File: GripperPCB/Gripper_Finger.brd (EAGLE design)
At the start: 26.6 x 20 mm, 6 parts, among them IC1 ATMEGA328PB-AU

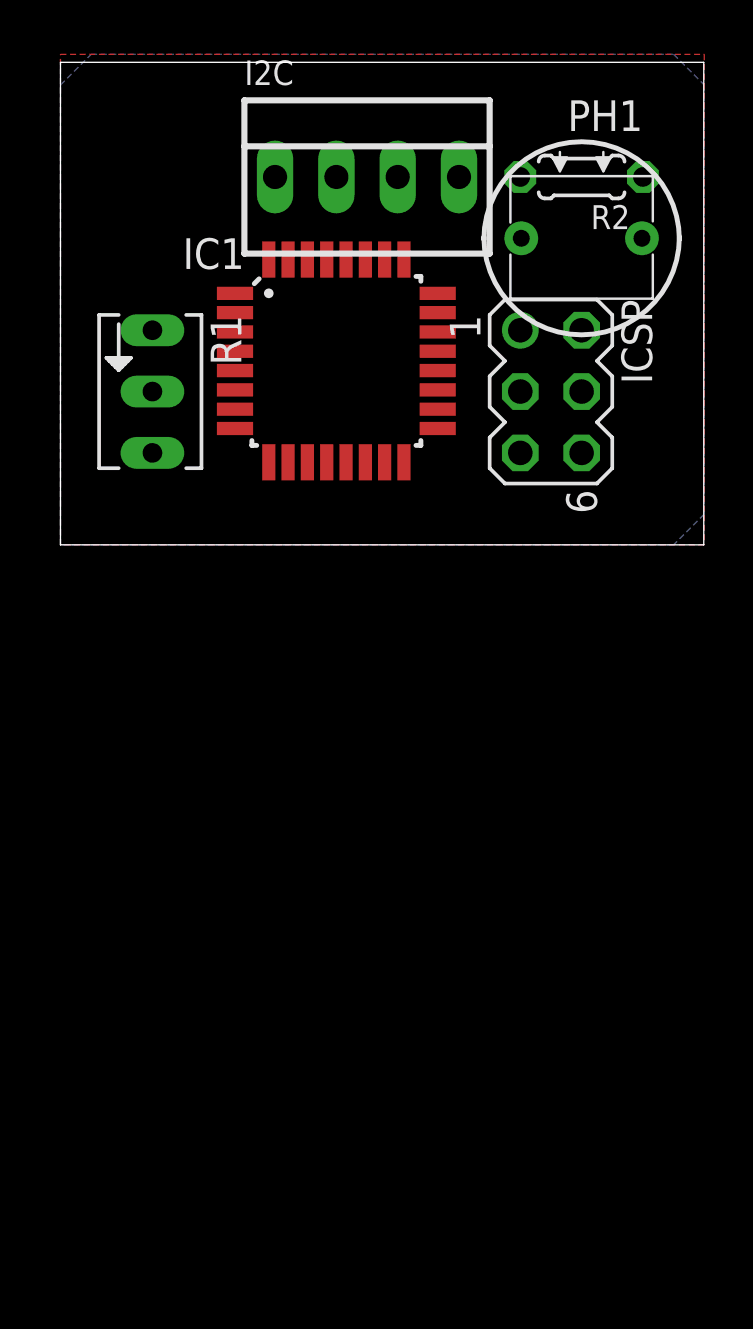
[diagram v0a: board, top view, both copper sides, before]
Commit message: board update with l293d
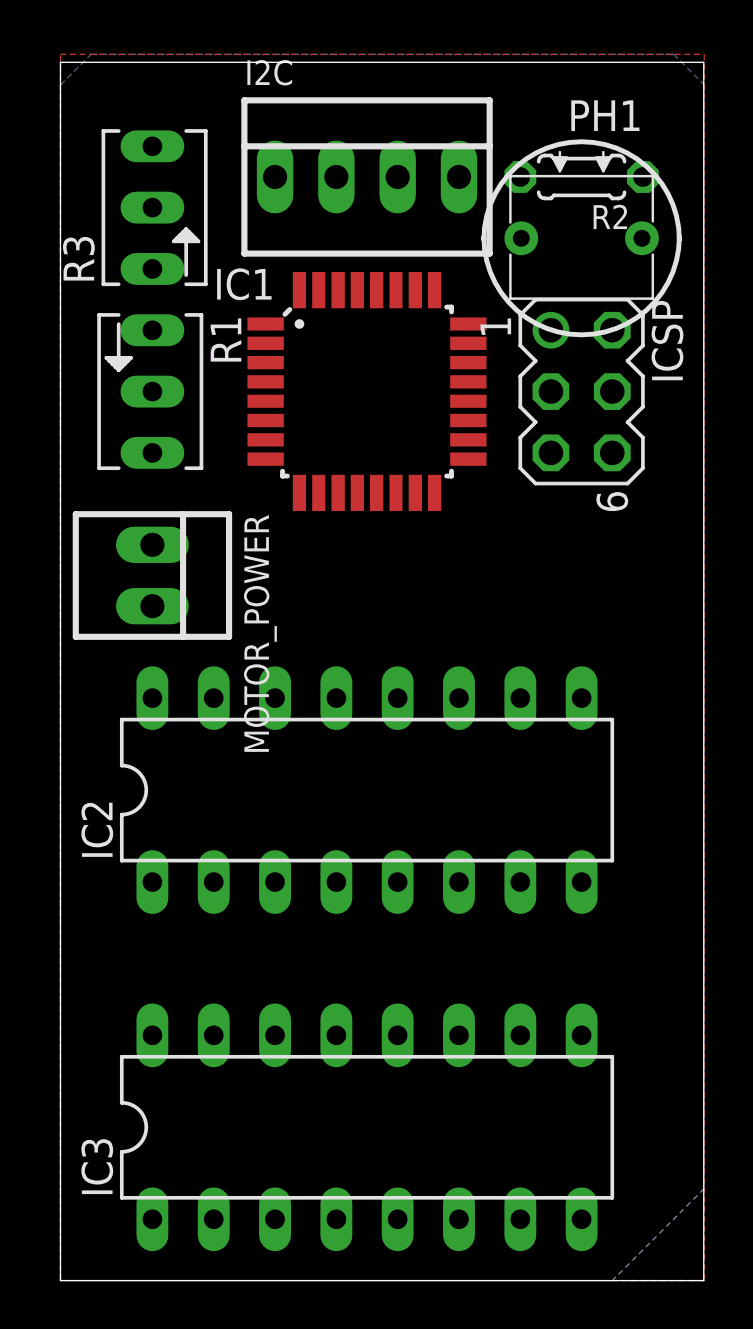
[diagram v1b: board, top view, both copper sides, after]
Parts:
- added IC2, IC3: L293D, st-microelectronics:DIL16
- added MOTOR_POWER: 22-23-2021, con-molex:22-23-2021
- added R3: (no value), pot:B64Y
- moved IC1 1.80 mm to (12.7, 6.35)
- moved ICSP 1.27 mm to (21.6, 6.35)
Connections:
- new net N$10: IC2.16, IC2.8, IC3.16, IC3.8, MOTOR_POWER.2
- new net N$9: IC1.25, R3.S
- net GND: now also IC2.12, IC2.13, IC2.4, IC2.5, IC3.12, IC3.13, IC3.4, IC3.5, MOTOR_POWER.1, R3.A
- net VCC: now also R3.E
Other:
- board size 26.6 x 20 mm -> 26.6 x 50.5 mm

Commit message: version 1.0.0 sent to engineering
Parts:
- added M1, M2, M3: 22-23-2021, con-molex:22-23-2021
- added R4: (no value), rcl:0204/5
- moved ICSP 67.3 mm to (34.3, 72.4)
- moved I2C 67.0 mm to (24.1, 81.3)
- moved IC1 67.0 mm to (24.1, 72.4)
- moved IC2 67.0 mm to (24.1, 55.9)
- moved R1 67.0 mm to (15.2, 72.4)
- moved R2 67.0 mm to (33.0, 81.3)
- moved R3 67.0 mm to (15.2, 80.0)
- moved MOTOR_POWER 67.0 mm to (15.2, 64.8)
- moved PH1 67.0 mm to (33.0, 78.7)
- moved IC3 63.3 mm to (24.1, 38.1), turned to 180 degrees
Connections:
- net N$1 renamed SCL
- net N$10 renamed MOTOR_POWER
- net N$2 renamed SDA
- net N$4 renamed SCK
- net N$5 renamed MISO
- net N$6 renamed MOSI
- net N$7 renamed LIGHT
- net N$8 renamed POT1
- net N$9 renamed POT2
- removed net N$3: IC1.29, ICSP.2
- new net M1A: IC2.14, M1.1
- new net M1B: IC2.11, M1.2
- new net M2A: IC2.3, M2.2
- new net M2B: IC2.6, M2.1
- new net M3A: IC3.6, M3.1
- new net M3B: IC3.3, M3.2
- new net N$11: IC1.32, IC2.10
- new net N$12: IC1.1, IC2.9
- new net N$13: IC1.2, IC2.15
- new net N$20: IC1.9, IC2.1
- new net N$21: IC1.10, IC2.2
- new net N$22: IC1.11, IC2.7
- new net N$23: IC1.13, IC3.7
- new net N$24: IC1.12, IC3.2
- new net N$25: IC1.14, IC3.1
- new net RESET: IC1.29, ICSP.2, R4.1
- net VCC: now also R4.2
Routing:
- net MOTOR_POWER: track 0.00 -> 66.4 mm
- net VCC: track 0.00 -> 52.7 mm
- net N$23: track 0.00 -> 41.1 mm, vias 0 -> 1
- net N$25: track 0.00 -> 38.9 mm
- net N$24: track 0.00 -> 29.6 mm, vias 0 -> 1
- net N$11: track 0.00 -> 23.2 mm, vias 0 -> 1
- net N$22: track 0.00 -> 23.0 mm, vias 0 -> 1
- net N$12: track 0.00 -> 22.2 mm, vias 0 -> 1
- net RESET: track 0.00 -> 21.1 mm, vias 0 -> 1
- net POT2: track 0.00 -> 20.4 mm
- net N$20: track 0.00 -> 19.4 mm
- net POT1: track 0.00 -> 19.1 mm, vias 0 -> 1
- net N$21: track 0.00 -> 19.1 mm
- net N$13: track 0.00 -> 18.5 mm, vias 0 -> 1
- net M1A: track 0.00 -> 15.9 mm
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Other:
- board size 26.6 x 50.5 mm -> 27.5 x 56.9 mm

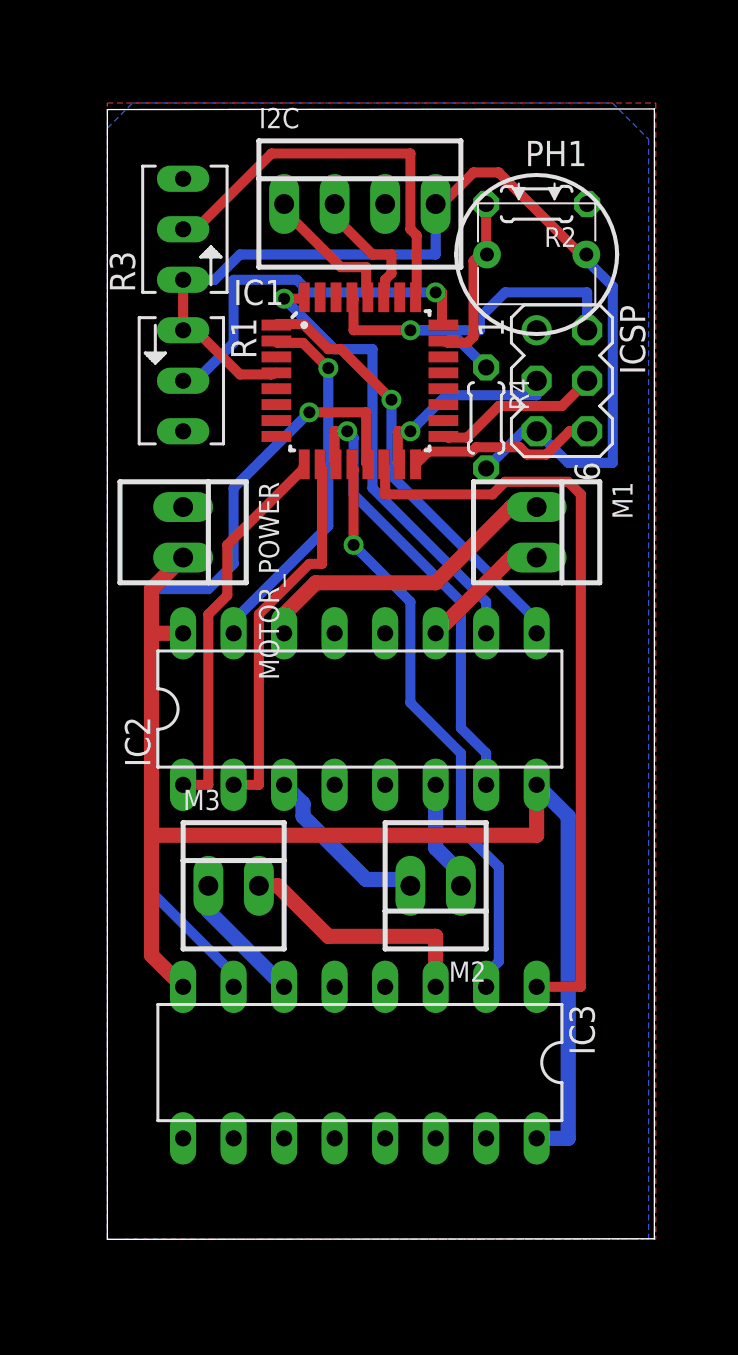
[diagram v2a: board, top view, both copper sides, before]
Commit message: added crystal
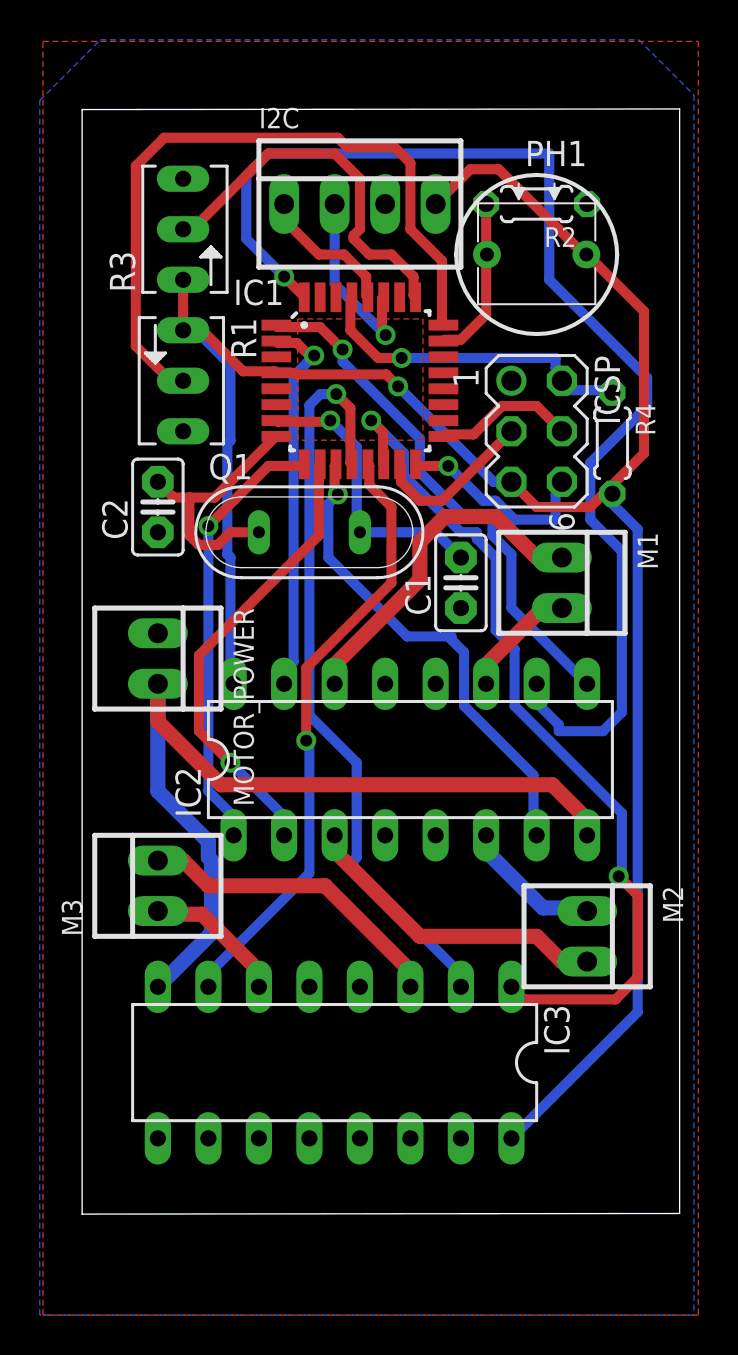
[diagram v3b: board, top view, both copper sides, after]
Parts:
- added C1, C2: (no value), capacitor-wima:C2.5-2
- added Q1: (no value), special:QS
- moved M2 8.03 mm to (35.6, 44.5), turned to 270 degrees
- moved R4 6.48 mm to (36.8, 69.2)
- moved MOTOR_POWER 6.48 mm to (14.0, 58.4)
- moved M3 3.81 mm to (14.0, 47.0), turned to 90 degrees
- moved IC2 3.59 mm to (26.7, 53.3)
- moved ICSP 2.84 mm to (33.0, 69.8)
- moved M1 2.84 mm to (34.3, 62.2)
- moved IC3 1.27 mm to (22.9, 38.1)
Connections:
- net N$11 renamed M1BSIG
- net N$12 renamed M1E
- net N$13 renamed M1ASIG
- net N$20 renamed M2E
- net N$21 renamed M2ASIG
- net N$22 renamed M2BSIG
- net N$23 renamed M3ASIG
- net N$24 renamed M3BSIG
- net N$25 renamed M3E
- new net CRYSTAL1: C2.2, IC1.8, Q1.1
- new net CRYSTAL2: C1.2, IC1.7, Q1.2
- net GND: now also C1.1, C2.1, IC3.10, IC3.15, IC3.9
- net MOTOR_POWER: no longer IC2.16, IC3.16
- net VCC: now also IC2.16, IC3.16
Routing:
- net VCC: track 52.7 -> 107.3 mm, vias 0 -> 1
- net M1BSIG: track 23.2 -> 61.4 mm
- net MOTOR_POWER: track 66.4 -> 43.8 mm
- net POT1: track 19.1 -> 35.9 mm, vias 1 -> 0
- net CRYSTAL2: track 0.00 -> 14.6 mm, vias 0 -> 1
- net CRYSTAL1: track 0.00 -> 13.4 mm
- net M3ASIG: track 41.1 -> 30.7 mm
- net M3BSIG: track 29.6 -> 38.0 mm
- net M2A: track 9.01 -> 15.8 mm
- net M3E: track 38.9 -> 43.7 mm, vias 0 -> 2
- net M1E: track 22.2 -> 26.6 mm
- net RESET: track 21.1 -> 16.9 mm
- net M2ASIG: track 19.1 -> 23.0 mm, vias 0 -> 1
- net M3B: track 12.5 -> 15.8 mm
- net SDA: track 6.57 -> 9.67 mm, vias 0 -> 1
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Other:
- board size 27.5 x 56.9 mm -> 30.1 x 55.6 mm

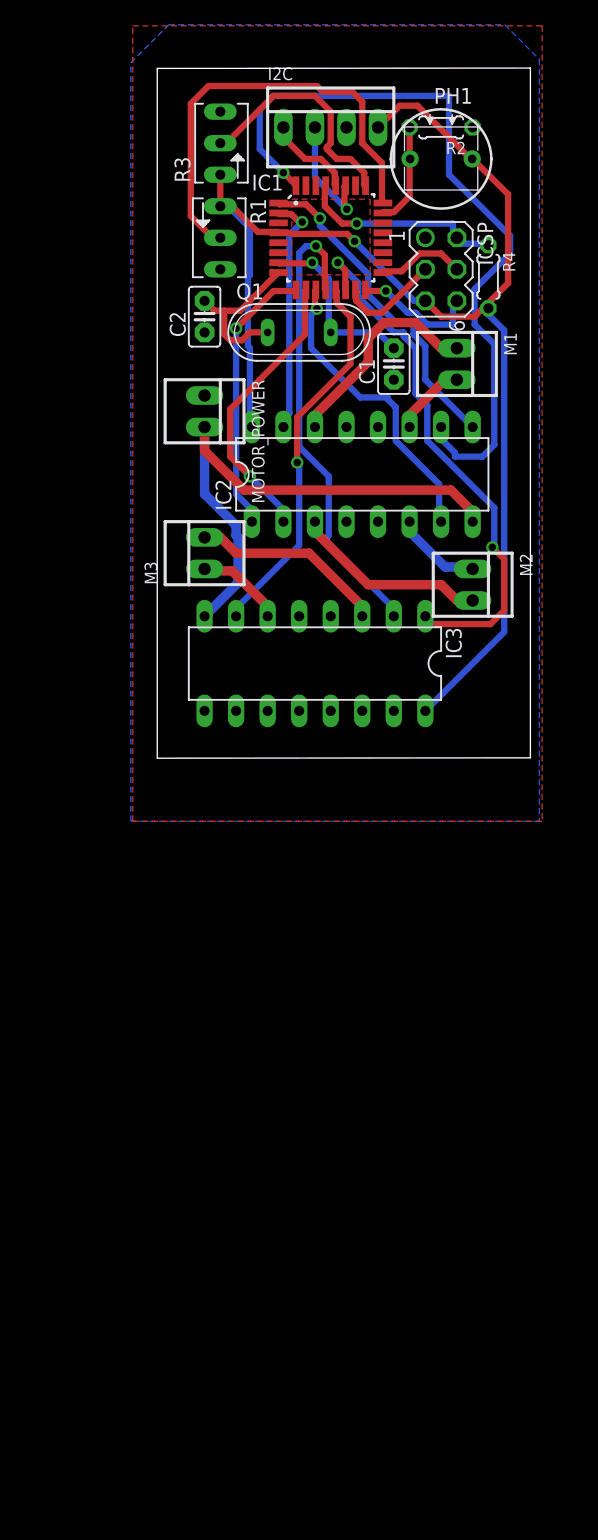
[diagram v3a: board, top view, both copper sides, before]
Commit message: layout with hole in rastnet under the uC
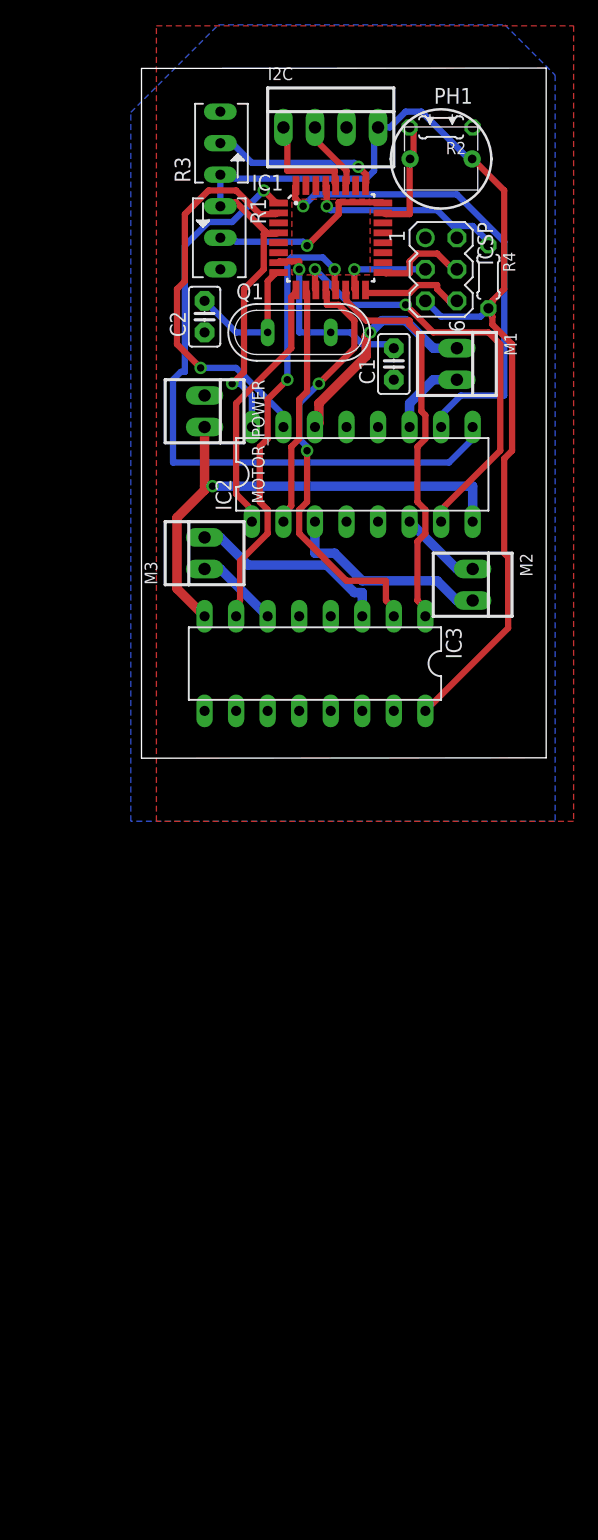
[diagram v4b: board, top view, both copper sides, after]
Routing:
- net M1E: track 26.6 -> 53.7 mm
- net M1BSIG: track 61.4 -> 39.2 mm
- net POT1: track 35.9 -> 15.4 mm, vias 0 -> 1
- net M1ASIG: track 19.3 -> 31.8 mm
- net M3E: track 43.7 -> 32.0 mm, vias 2 -> 0
- net M2BSIG: track 24.6 -> 35.4 mm, vias 1 -> 2
- net M3ASIG: track 30.7 -> 36.8 mm, vias 1 -> 2
- net POT2: track 19.0 -> 13.7 mm, vias 0 -> 1
- net SDA: track 9.67 -> 5.75 mm, vias 1 -> 0
- net M2ASIG: track 23.0 -> 19.5 mm, vias 1 -> 0
- net M3BSIG: track 38.0 -> 35.2 mm, vias 1 -> 2
- net MOTOR_POWER: track 43.8 -> 41.5 mm, vias 0 -> 1
- net CRYSTAL1: track 13.4 -> 11.4 mm
- net VCC: track 107.3 -> 109.2 mm
- net MISO: track 10.2 -> 8.53 mm, vias 1 -> 0
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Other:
- board size 30.1 x 55.6 mm -> 32.6 x 55.6 mm
